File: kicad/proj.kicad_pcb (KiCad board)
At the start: 2 copper layers, 22 parts, among them J1 XLR, J2 XLR, J3 CONN_PWR, J4 CONN_S1A, J5 CONN_S1B, U1 INA217, U2 NE5532

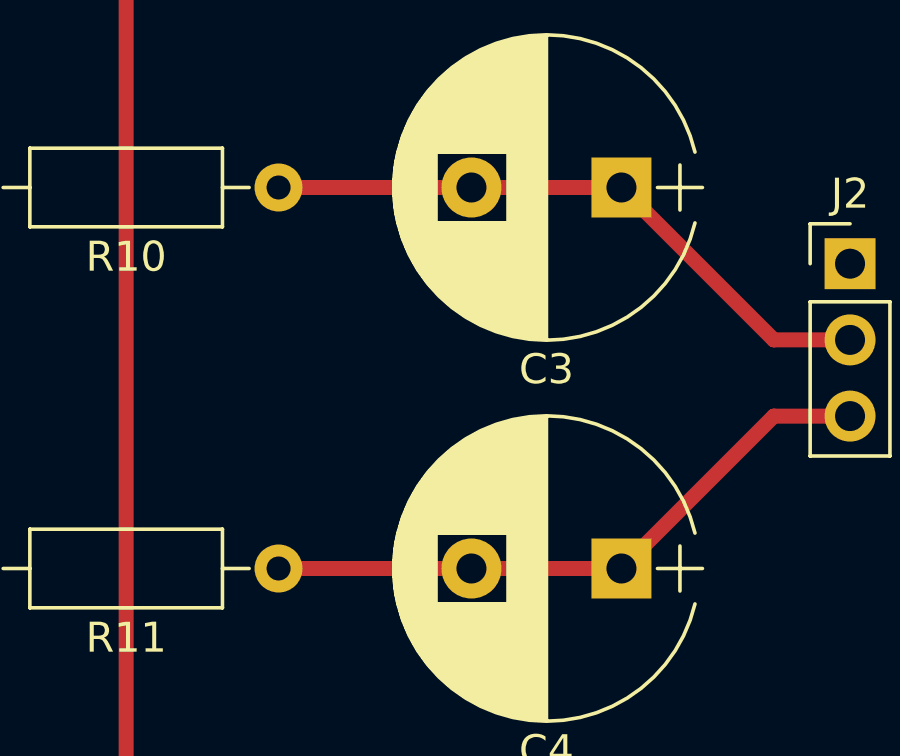
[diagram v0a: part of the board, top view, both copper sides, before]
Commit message: Change C1-4 to non-polar and connected XLR pin 1s to chassis, only GND at input
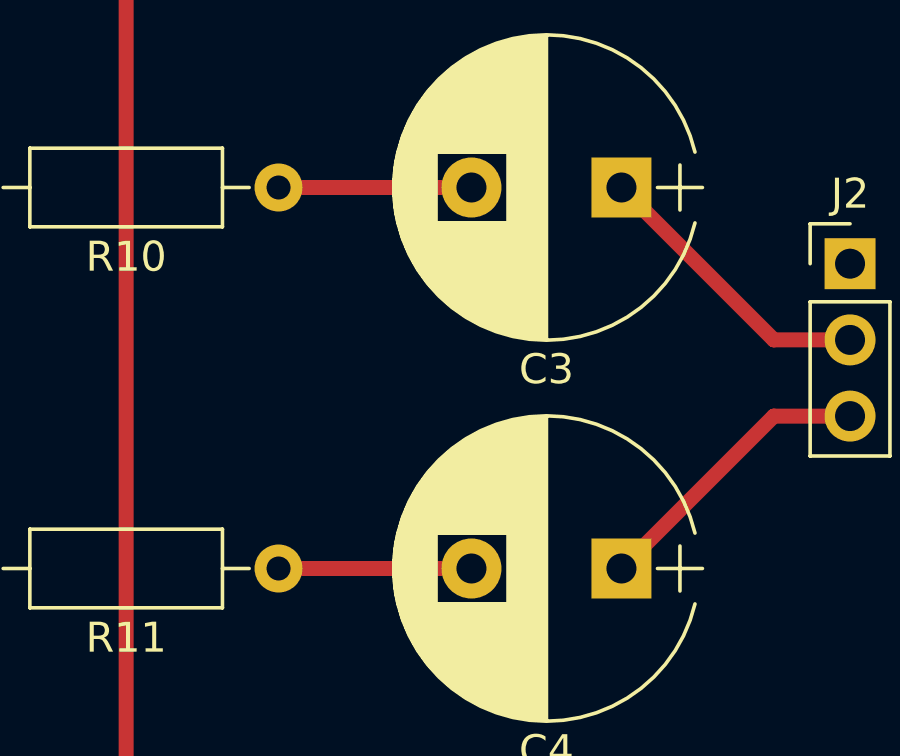
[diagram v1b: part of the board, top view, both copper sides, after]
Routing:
- net Net-(C4-Pad2): track 11.4 -> 6.43 mm
- net Net-(C3-Pad2): track 11.4 -> 6.43 mm
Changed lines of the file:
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@@
   (general
     (links 40)
-    (no_connects 2)
-    (area 0 0 0 0)
+    (no_connects 0)
+    (area 90.17 83.10619 193.040001 128.793333)
     (thickness 1.6)
     (drawings 0)
@@
       (drillshape 0)
       (scaleselection 1)
-      (outputdirectory ./))
+      (outputdirectory exports/))
   )
   (net 0 "")
@@
   (segment (start 111.76 106.68) (end 114.3 106.68) (width 0.5) (layer F.Cu) (net 4))
   (segment (start 114.3 106.68) (end 121.92 106.68) (width 0.5) (layer F.Cu) (net 4))
+  (segment (start 181.53 99.06) (end 181.61 99.06) (width 0.5) (layer F.Cu) (net 5) (status 30))
+  (segment (start 181.61 99.06) (end 186.69 104.14) (width 0.5) (layer F.Cu) (net 5) (status 10))
   (segment (start 186.69 104.14) (end 189.23 104.14) (width 0.5) (layer F.Cu) (net 5))
-  (segment (start 181.53 99.06) (end 181.61 99.06) (width 0.5) (layer F.Cu) (net 5))
-  (segment (start 181.61 99.06) (end 186.69 104.14) (width 0.5) (layer F.Cu) (net 5))
-  (segment (start 170.18 99.06) (end 181.61 99.06) (width 0.5) (layer F.Cu) (net 6) (status 20))
-  (segment (start 186.69 106.68) (end 189.23 106.68) (width 0.5) (layer F.Cu) (net 7))
+  (segment (start 170.18 99.06) (end 176.61 99.06) (width 0.5) (layer F.Cu) (net 6) (status C00000))
   (segment (start 181.53 111.76) (end 181.61 111.76) (width 0.5) (layer F.Cu) (net 7))
   (segment (start 181.61 111.76) (end 186.69 106.68) (width 0.5) (layer F.Cu) (net 7))
-  (segment (start 170.18 111.76) (end 181.61 111.76) (width 0.5) (layer F.Cu) (net 8) (status 20))
+  (segment (start 186.69 106.68) (end 189.23 106.68) (width 0.5) (layer F.Cu) (net 7))
+  (segment (start 170.18 111.76) (end 176.61 111.76) (width 0.5) (layer F.Cu) (net 8) (status C00000))
   (segment (start 119.26 123.19) (end 119.38 123.07) (width 0.5) (layer F.Cu) (net 9))
   (segment (start 119.38 123.07) (end 119.38 123.19) (width 0.5) (layer F.Cu) (net 9))
